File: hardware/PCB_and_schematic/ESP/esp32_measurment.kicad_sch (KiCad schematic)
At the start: 104 parts, among them J1 DB9_Socket, J13 H2_SENSOR, J14 7SEG_DISP, J15 CO_SENSOR, J17 LCD_DISP, J20 DHT22, J3 BATTERY_SHUNT, J4 DC_LINE_OUTPUT, J6 RS485, J8 OR_OR_Smoke_sensor, K1 Relay_SPST-NO, Q1 BSS138, Q2 BSS138, Q3 BC817, Q4 BC817, Q5 BC817, Q6 BC817, Q7 BC817, Q8 NPN, Q9 BC817, SW1 SW_Push, U1 ESP32_DevKit_V1_DOIT, U10 UP7760, U19 PCF8574, U2 INA226, U3 MAX232, U7 AMS1117-5.0, U8 ST485, U9 INA226

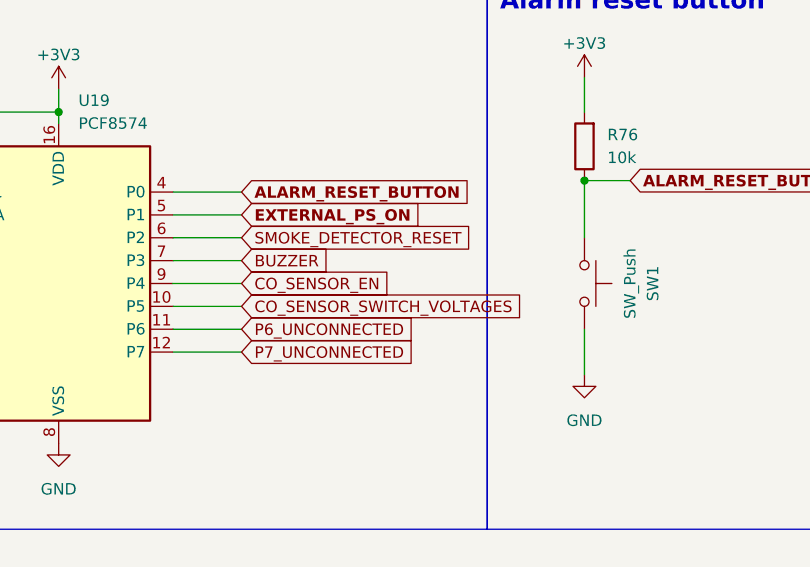
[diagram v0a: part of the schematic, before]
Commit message: esp pcb route
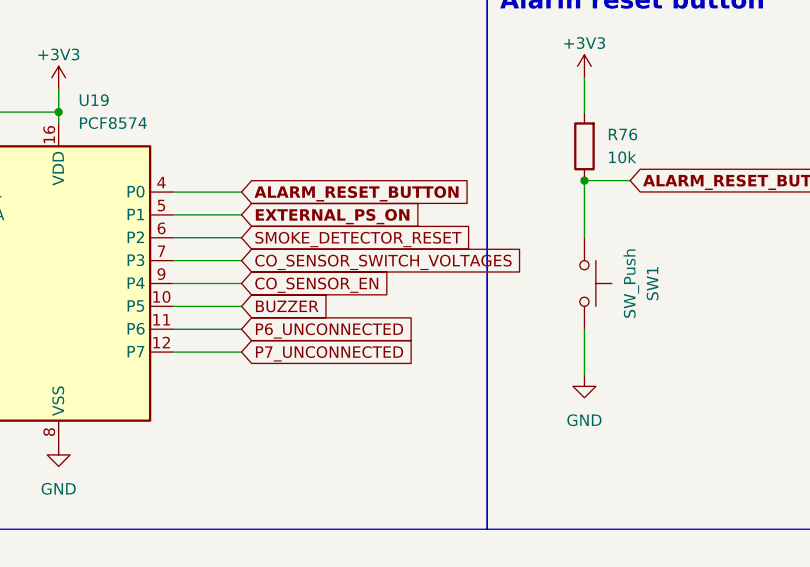
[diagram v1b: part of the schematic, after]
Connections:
- net BUZZER: now also U19.10 (P5); no longer U19.7 (P3)
- net CO_SENSOR_SWITCH_VOLTAGES: now also U19.7 (P3); no longer U19.10 (P5)
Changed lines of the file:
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@@
 	(global_label "CO_SENSOR_SWITCH_VOLTAGES"
 		(shape input)
-		(at 101.6 266.7 0)
+		(at 101.6 261.62 0)
 		(fields_autoplaced yes)
 		(effects
@@
 		)
 		(property "Intersheetrefs" "${INTERSHEET_REFS}"
-			(at 133.5532 266.7 0)
+			(at 133.5532 261.62 0)
 			(effects
 				(font
@@
 	(global_label "BUZZER"
 		(shape input)
-		(at 101.6 261.62 0)
+		(at 101.6 266.7 0)
 		(fields_autoplaced yes)
 		(effects
@@
 		)
 		(property "Intersheetrefs" "${INTERSHEET_REFS}"
-			(at 112.0237 261.62 0)
+			(at 112.0237 266.7 0)
 			(effects
 				(font

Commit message: corase routing for esp doce
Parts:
- added D6: LL4148, Diode_SMD:D_MiniMELF, symbol Diode:LL4148
- Q8: footprint Package_TO_SOT_THT:TO-92_Inline_Wide -> My-Footprints:TO-92_Inline_Wide
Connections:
- net +BATT_24V: now also D6.1 (K)
- net CO_SENSOR_EN: now also U19.7 (P3); no longer U19.9 (P4)
- net CO_SENSOR_SWITCH_VOLTAGES: now also U19.6 (P2); no longer U19.7 (P3)
- net SMOKE_DETECTOR_RESET: now also U19.9 (P4); no longer U19.6 (P2)
- net at K1.A2, Q8.1 (C): now also D6.2 (A)
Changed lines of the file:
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@@
 	)
 	(junction
+		(at 219.71 248.92)
+		(diameter 0)
+		(color 0 0 0 0)
+	)
+	(junction
 		(at 288.29 250.19)
 		(diameter 0)
@@
 	)
 	(junction
+		(at 219.71 266.7)
+		(diameter 0)
+		(color 0 0 0 0)
+	)
+	(junction
 		(at 199.39 194.31)
 		(diameter 0)
@@
 	(wire
 		(pts
+			(xy 208.28 254) (xy 208.28 248.92)
+		)
+		(stroke
+			(width 0)
+			(type default)
+		)
+	)
+	(wire
+		(pts
 			(xy 397.51 90.17) (xy 401.32 90.17)
 		)
@@
 	(wire
 		(pts
-			(xy 219.71 237.49) (xy 219.71 250.19)
+			(xy 219.71 237.49) (xy 219.71 248.92)
 		)
 		(stroke
@@
 	(wire
 		(pts
-			(xy 219.71 265.43) (xy 219.71 271.78)
+			(xy 219.71 265.43) (xy 219.71 266.7)
 		)
 		(stroke
@@
 	(wire
 		(pts
+			(xy 219.71 266.7) (xy 219.71 271.78)
+		)
+		(stroke
+			(width 0)
+			(type default)
+		)
+	)
+	(wire
+		(pts
 			(xy 232.41 101.6) (xy 232.41 91.44)
 		)
@@
 	(wire
 		(pts
+			(xy 208.28 266.7) (xy 208.28 261.62)
+		)
+		(stroke
+			(width 0)
+			(type default)
+		)
+	)
+	(wire
+		(pts
 			(xy 422.91 161.29) (xy 429.26 161.29)
 		)
@@
 	(wire
 		(pts
+			(xy 208.28 248.92) (xy 219.71 248.92)
+		)
+		(stroke
+			(width 0)
+			(type default)
+		)
+	)
+	(wire
+		(pts
 			(xy 397.51 207.01) (xy 402.59 207.01)
 		)
@@
 	(wire
 		(pts
+			(xy 219.71 266.7) (xy 208.28 266.7)
+		)
+		(stroke
+			(width 0)
+			(type default)
+		)
+	)
+	(wire
+		(pts
 			(xy 316.23 147.32) (xy 304.8 147.32)
 		)
@@
 	(wire
 		(pts
+			(xy 219.71 248.92) (xy 219.71 250.19)
+		)
+		(stroke
+			(width 0)
+			(type default)
+		)
+	)
+	(wire
+		(pts
 			(xy 527.05 160.02) (xy 527.05 163.83)
 		)
@@
 	(global_label "SMOKE_DETECTOR_RESET"
 		(shape input)
-		(at 101.6 259.08 0)
+		(at 101.6 264.16 0)
 		(fields_autoplaced yes)
 		(effects
@@
 		)
 		(property "Intersheetrefs" "${INTERSHEET_REFS}"
-			(at 128.0496 259.08 0)
+			(at 128.0496 264.16 0)
 			(effects
 				(font
@@
 	(global_label "CO_SENSOR_SWITCH_VOLTAGES"
 		(shape input)
-		(at 101.6 261.62 0)
+		(at 101.6 259.08 0)
 		(fields_autoplaced yes)
 		(effects
@@
 		)
 		(property "Intersheetrefs" "${INTERSHEET_REFS}"
-			(at 133.5532 261.62 0)
+			(at 133.5532 259.08 0)
 			(effects
 				(font
@@
 	(global_label "CO_SENSOR_EN"
 		(shape input)
-		(at 101.6 264.16 0)
+		(at 101.6 261.62 0)
 		(fields_autoplaced yes)
 		(effects
@@
 		)
 		(property "Intersheetrefs" "${INTERSHEET_REFS}"
-			(at 119.0994 264.16 0)
+			(at 119.0994 261.62 0)
 			(effects
 				(font
@@
 			)
 		)
-		(property "Footprint" "Package_TO_SOT_THT:TO-92_Inline_Wide"
+		(property "Footprint" "My-Footprints:TO-92_Inline_Wide"
 			(at 280.67 276.86 0)
 			(effects
@@
 					(unit 1)
 				)
+			)
+		)
+	)
+	(symbol
+		(lib_id "Diode:LL4148")
+		(at 208.28 257.81 270)
+		(unit 1)
+		(exclude_from_sim no)
+		(in_bom yes)
+		(on_board yes)
+		(dnp no)
+		(fields_autoplaced yes)
+		(property "Reference" "D6"
+			(at 210.82 256.5399 90)
+			(effects
+				(font
+					(size 1.27 1.27)
+				)
+				(justify left)
+			)
+		)
+		(property "Value" "LL4148"
+			(at 210.82 259.0799 90)
+			(effects
+				(font
+					(size 1.27 1.27)
+				)
+				(justify left)
+			)
+		)
+		(property "Footprint" "Diode_SMD:D_MiniMELF"
+			(at 203.835 257.81 0)
+			(effects
+				(font
+					(size 1.27 1.27)
+				)
+				(hide yes)
+			)
+		)
+		(property "Datasheet" "http://www.vishay.com/docs/85557/ll4148.pdf"
+			(at 208.28 257.81 0)
+			(effects
+				(font
+					(size 1.27 1.27)
+				)
+				(hide yes)
+			)
+		)
+		(property "Description" "100V 0.15A standard switching diode, MiniMELF"
+			(at 208.28 257.81 0)
+			(effects
+				(font
+					(size 1.27 1.27)
+				)
+				(hide yes)
+			)
+		)
+		(property "Sim.Device" "D"
+			(at 208.28 257.81 0)
+			(effects
+				(font
+					(size 1.27 1.27)
+				)
+				(hide yes)
+			)
+		)
+		(property "Sim.Pins" "1=K 2=A"
+			(at 208.28 257.81 0)
+			(effects
+				(font
+					(size 1.27 1.27)
+				)
+				(hide yes)
+			)
+		)
+		(pin "1"
+		)
+		(pin "2"
+		)
+		(instances
+			(project "ESP32_master"
+				(path "/555ba40f-9abb-4b99-82c6-07e888fda9fd/a8064d67-baba-4afe-84af-1260f43bc5ee"
+					(reference "D6")
+					(unit 1)
+				)

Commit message: Fineing ESP PCB
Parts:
- removed J3: BATTERY_SHUNT, Connector_JST:JST_EH_B4B-EH-A_1x04_P2.50mm_Vertical, symbol Connector_Generic:Conn_01x04
- removed J8: OR_OR_Smoke_sensor, My-Footprints-connectors:Screw-Terminal-5.00mm-3pin, symbol Connector:Screw_Terminal_01x03
- added C19: 1n, Resistor_SMD:R_0805_2012Metric_Pad1.20x1.40mm_HandSolder, symbol Device:C
- added J1: OR-OR SMOKE SENSOR, Connector_JST:JST_EH_B3B-EH-A_1x03_P2.50mm_Vertical, symbol Connector_Generic:Conn_01x03
- added J14: MAIN_BATT_SHUNT, Connector_JST:JST_EH_B3B-EH-A_1x03_P2.50mm_Vertical, symbol Connector_Generic:Conn_01x03
- added J7: MAIN_BATT_+24V, My-Footprints-connectors:Screw-Terminal-P2-rast-5mm-6,7x30, symbol Connector_Generic:Conn_01x02
- added JP1: Jumper_2_Bridged, Jumper:SolderJumper-2_P1.3mm_Bridged2Bar_Pad1.0x1.5mm, symbol Jumper:Jumper_2_Bridged
- added R60, R61: 100R, Resistor_SMD:R_0805_2012Metric_Pad1.20x1.40mm_HandSolder, symbol Device:R
- renumbered C38 to C1, C22 to C10, C21 to C11, C1 to C12, C20 to C13, C9 to C14, C3 to C15, C4 to C16, C5 to C17, C29 to C2, C27 to C3, C24 to C4, C25 to C5, C26 to C6, C23 to C7, C30 to C8, C2 to C9, D16 to D1, D28 to D2, D27 to D3, D25 to D4, D1 to D5, D2 to D6, D6 to D7, D24 to D8, D19 to D9, F8 to F1, F6 to F3, J13 to J10, J17 to J2, J14 to J3, J6 to J4, J20 to J5, J4 to J6, J1 to J8, J15 to J9, D5 to LED1, D4 to LED2, MOD2 to MOD1, MOD1 to MOD2, Q5 to Q1, Q4 to Q2, Q8 to Q4, Q2 to Q5, Q1 to Q6, Q6 to Q7, Q7 to Q8, R29 to R1, R12 to R10, R13 to R11, R14 to R12, R77 to R13, R33 to R14, R1 to R15, R32 to R16, R31 to R17, R78 to R18, R17 to R19, R28 to R2, R34 to R20, R84 to R21, R79 to R22, R4 to R23, R21 to R25, R5 to R26, R20 to R27, R2 to R28, R18 to R29, R26 to R3, R3 to R30, R19 to R31, R22 to R32, R23 to R33, R37 to R34, R38 to R35, R39 to R36, R40 to R37, R25 to R38, R30 to R39, R73 to R4, R41 to R40, R42 to R41, R72 to R5, R76 to R6, R88 to R7, R87 to R8, R85 to R9, U19 to U1, U8 to U2, U7 to U3, U1 to U4, U9 to U5, U3 to U6, U2 to U7, U10 to U8
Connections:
- net +20V: now also J1.3 (Pin_3)
- net GND: now also J14.1 (Pin_1), JP1.2 (B); no longer J6.2 (Pin_2), J6.4 (Pin_4), J6.6 (Pin_6), MOD1.1 (IN-), MOD1.3 (OUT-)
- net RS485_A: now also J4.2 (Pin_2); no longer J4.3 (Pin_3)
- net RS485_B: now also J4.3 (Pin_3); no longer J4.2 (Pin_2)
- net at Q1.3 (C): now also J1.1 (Pin_1)
- net at R2.1: now also J1.2 (Pin_2)
- net at U7.10 (Vin+): now also C19.1, R60.2
- net at U7.8 (Vbus), U7.9 (Vin-): now also C19.2, R61.2
- net at F3.2: now also J7.2 (Pin_2)
- new net: J14.2 (Pin_2), R61.1
- new net: J14.3 (Pin_3), R60.1
- new net GNDA: J6.2 (Pin_2), J6.4 (Pin_4), J6.6 (Pin_6), J7.1 (Pin_1), JP1.1 (A), MOD1.1 (IN-), MOD1.3 (OUT-)
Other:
- moved on the sheet: F3

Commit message: change relay
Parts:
- K1: footprint Relay_THT:Relay_SPST_Omron_G2RL-1A -> My-Footprints:G5G-1A-DT1
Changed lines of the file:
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@@
 			)
 		)
-		(property "Footprint" "Relay_THT:Relay_SPST_Omron_G2RL-1A"
+		(property "Footprint" "My-Footprints:G5G-1A-DT1"
 			(at 236.22 259.08 0)
 			(effects

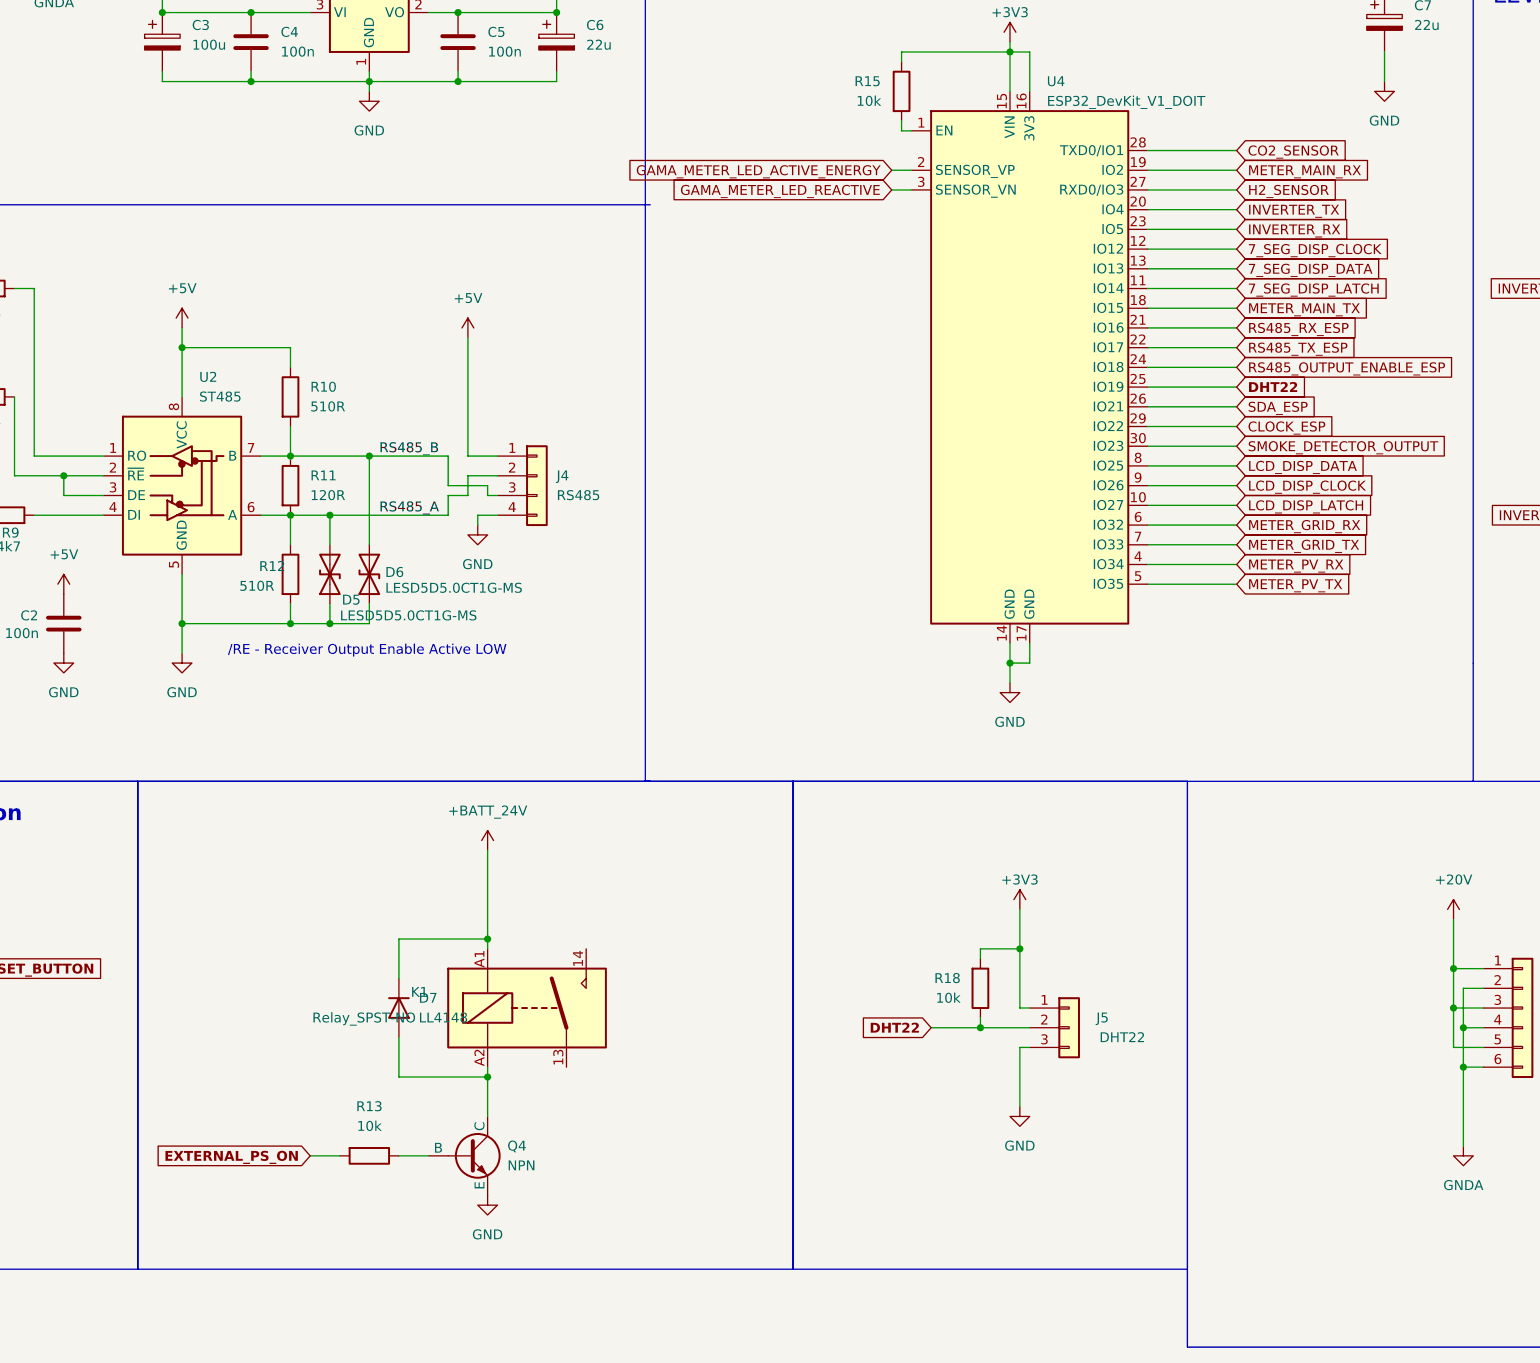
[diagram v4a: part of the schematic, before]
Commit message: ESP relay circut change
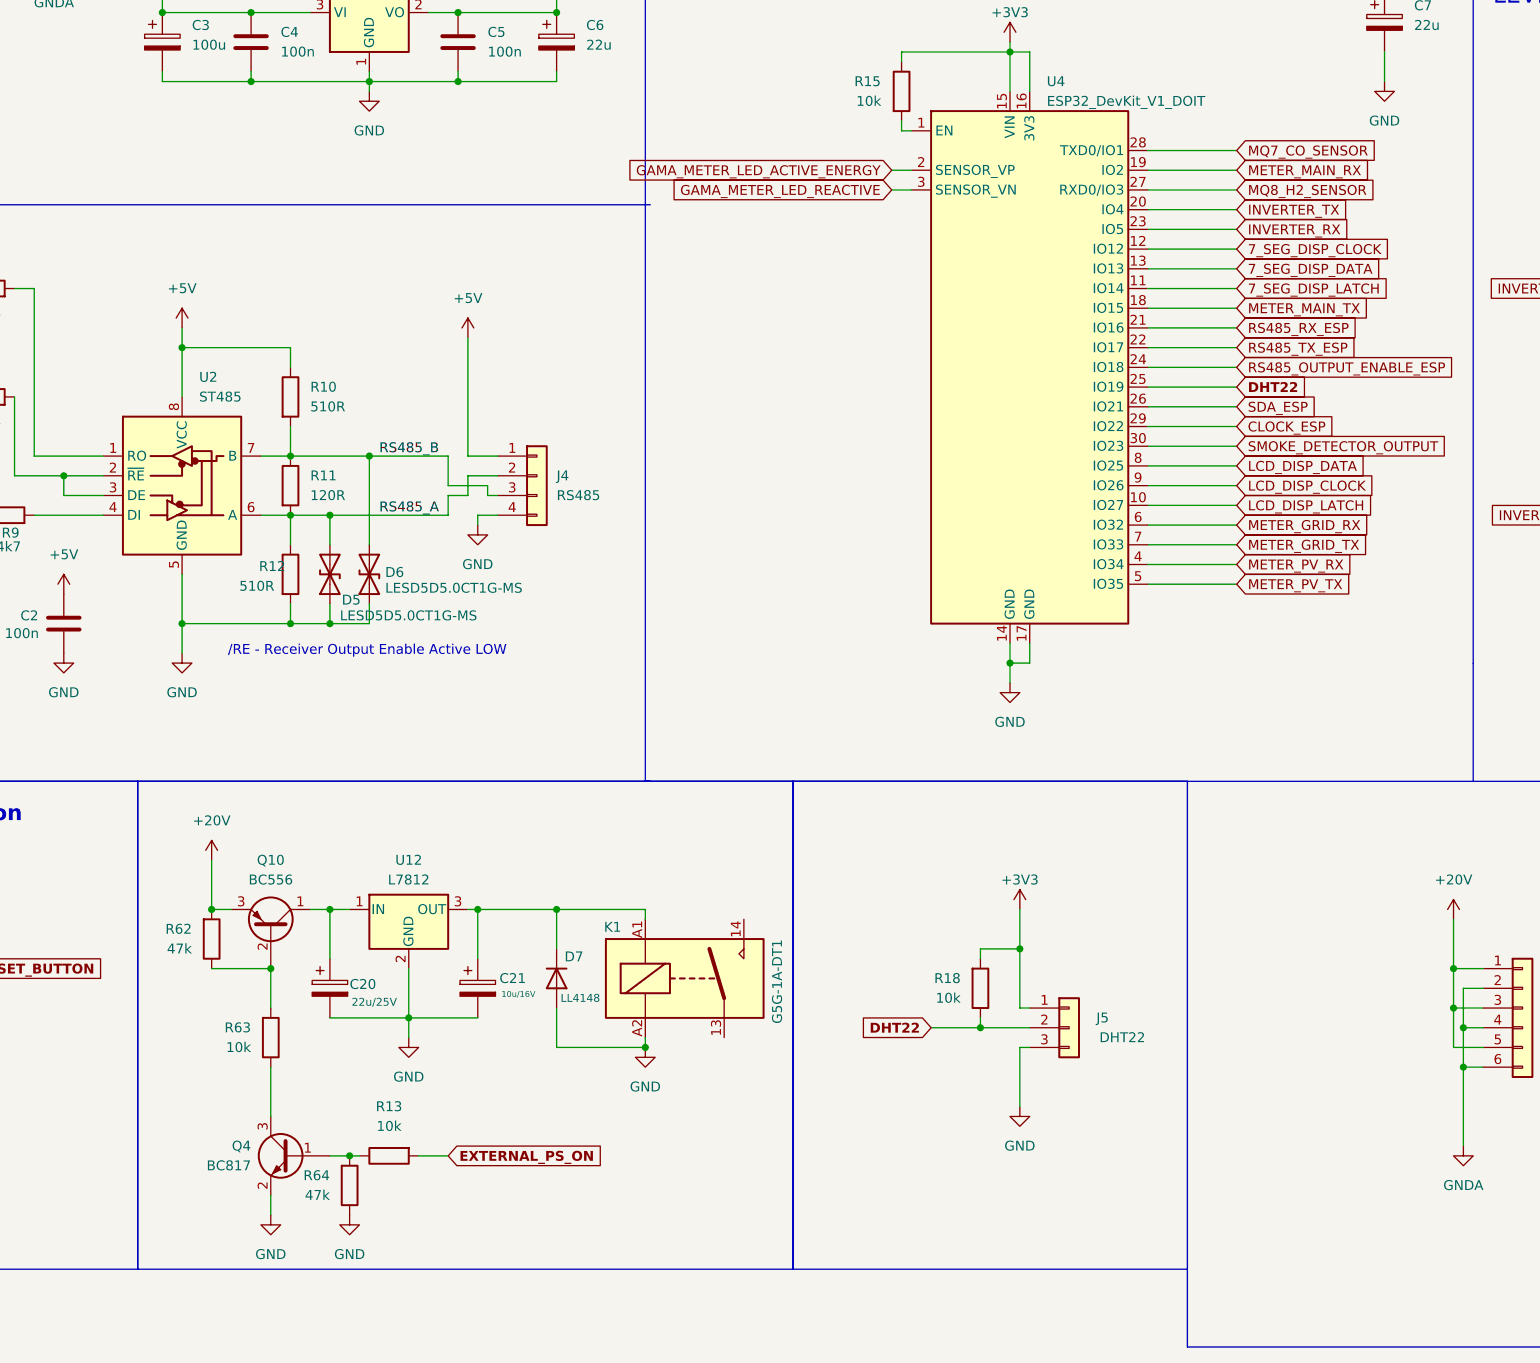
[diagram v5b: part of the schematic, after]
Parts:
- removed Q4: NPN, My-Footprints:TO-92_Inline_Wide, symbol Simulation_SPICE:NPN
- added C20: 22u/25V, Capacitor_Tantalum_SMD:CP_EIA-3528-21_Kemet-B, symbol Device:C_Polarized
- added C21: 10u/16V, Capacitor_Tantalum_SMD:CP_EIA-3528-21_Kemet-B, symbol Device:C_Polarized
- added Q10: BC556, Package_TO_SOT_THT:TO-92_Inline, symbol Transistor_BJT:BC556
- added Q4: BC817, Package_TO_SOT_SMD:SOT-23, symbol Transistor_BJT:BC817
- added R62, R64: 47k, Resistor_SMD:R_0805_2012Metric_Pad1.20x1.40mm_HandSolder, symbol Device:R
- added R63: 10k, Resistor_SMD:R_0805_2012Metric_Pad1.20x1.40mm_HandSolder, symbol Device:R
- added U12: L7812, My-Footprints:TO-220-3_V_Thick_Pads, symbol Regulator_Linear:L7812
- K1: value Relay_SPST-NO -> G5G-1A-DT1
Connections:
- net CO2_SENSOR is gone; now on net MQ7_CO_SENSOR: U4.28 (TXD0/IO1)
- net H2_SENSOR is gone; now on net MQ8_H2_SENSOR: U4.27 (RXD0/IO3)
- net +20V: now also Q10.3 (E), R62.2
- net +BATT_24V: no longer D7.1 (K), K1.A1
- net GND: now also D7.2 (A), K1.A2, C20.2, C21.2, Q4.2 (E), R64.1, U12.2 (GND)
- net at R13.1: now also Q4.1 (B), R64.2
- new net: C21.1, D7.1 (K), K1.A1, U12.3 (OUT)
- new net: Q10.2 (B), R62.1, R63.2
- new net: Q4.3 (C), R63.1
- new net: C20.1, Q10.1 (C), U12.1 (IN)
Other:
- moved on the sheet: D7, K1, R13

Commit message: Change MAX232 to MAX3232
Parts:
- removed U6: MAX232, Package_SO:SOIC-16W_5.3x10.2mm_P1.27mm, symbol Interface_UART:MAX232
- added R65, R66: 0R, Resistor_SMD:R_0805_2012Metric_Pad1.20x1.40mm_HandSolder, symbol Device:R
- added U13: MAX3232, Package_SO:SO-16_3.9x9.9mm_P1.27mm, symbol Interface_UART:MAX3232
- J1, J14: footprint Connector_JST:JST_EH_B3B-EH-A_1x03_P2.50mm_Vertical -> Connector_JST:JST_XH_B3B-XH-A_1x03_P2.50mm_Vertical
- J4: footprint Connector_PinHeader_2.54mm:PinHeader_1x04_P2.54mm_Vertical -> Connector_JST:JST_XH_B4B-XH-A_1x04_P2.50mm_Vertical
- SW1: footprint Connector_PinHeader_2.54mm:PinHeader_1x02_P2.54mm_Vertical -> Connector_JST:JST_XA_B02B-XASK-1_1x02_P2.50mm_Vertical
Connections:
- net +3V3: now also R66.1
- net +5V: now also R65.1; no longer C10.2, C11.1, C13.2
- net GND: now also U13.15 (GND)
- net INV_RX_RS232: now also U13.7 (T2OUT)
- net INV_TX_RS232: now also U13.8 (R2IN)
- net at C13.1: now also U13.2 (VS+)
- net at C15.1: now also U13.4 (C2+)
- net at C15.2: now also U13.5 (C2-)
- net at R26.2: now also U13.13 (R1IN)
- net at R22.2: now also U13.9 (R2OUT)
- net at C14.2: now also U13.6 (VS-)
- net at R21.2: now also U13.10 (T2IN)
- net at C9.1: now also U13.1 (C1+)
- net at R23.1: now also U13.11 (T1IN)
- net at C9.2: now also U13.3 (C1-)
- new net: C10.2, C11.1, C13.2, R65.2, R66.2, U13.16 (VCC)

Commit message: Add SD card switcher circuit, some changes in pcb and schematic
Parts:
- added Q11, Q8: BC817, Package_TO_SOT_SMD:SOT-23, symbol Transistor_BJT:BC817
- added R41, R48: 10K, Resistor_SMD:R_0805_2012Metric_Pad1.20x1.40mm_HandSolder, symbol Device:R
- renumbered C8 to C10, C9 to C11, C10 to C12, C19 to C13, C11 to C14, C12 to C15, C13 to C16, C14 to C17, C15 to C18, C16 to C19, C17 to C20, C20 to C5, C5 to C6, C21 to C7, C6 to C8, C7 to C9, J9 to J10, J10 to J11, J14 to J8, J8 to J9, LED2 to LED1, LED1 to LED2, Q8 to Q10, Q9 to Q12, Q10 to Q4, Q4 to Q5, Q5 to Q6, Q6 to Q7, Q7 to Q9, R62 to R10, R63 to R11, R10 to R12, R11 to R13, R12 to R14, R64 to R15, R13 to R16, R14 to R17, R15 to R18, R16 to R19, R17 to R20, R18 to R21, R19 to R22, R20 to R23, R21 to R24, R22 to R25, R60 to R26, R61 to R27, R23 to R28, R24 to R29, R25 to R30, R26 to R31, R27 to R32, R28 to R33, R65 to R34, R29 to R35, R30 to R36, R66 to R37, R31 to R38, R32 to R39, R33 to R40, R34 to R42, R35 to R43, R36 to R44, R37 to R45, R38 to R46, R39 to R47, R40 to R49, R41 to R50, U12 to U4, U4 to U5, U5 to U6, U13 to U7, U7 to U8, U8 to U9
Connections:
- net GND: now also Q11.2 (E), Q8.2 (E)
- net P7_UNCONNECTED: now also R48.2
- net P6_UNCONNECTED renamed ALARM_SYREN
- net ALARM_SYREN: now also R41.2
- new net: Q8.1 (B), R41.1
- new net: Q11.1 (B), R48.1
- new net ALARM_SYREN_OUTPUT: Q8.3 (C)
- new net P7_UNCONNECTED_OUTPUT: Q11.3 (C)
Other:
- note added: "20V SCREW TERMINAL CONNECTORS"
- note added: "ALARM RESET BUTTON"
- note added: "CO AND H2 SENSORS"
- note added: "DHT22 CONNECTOR"
- note added: "EXTERNAL POWER SUPPLY RELAY"
- note removed: "Alarm reset button"
- moved on the sheet: J6, JE1, Q12, R49, R50
